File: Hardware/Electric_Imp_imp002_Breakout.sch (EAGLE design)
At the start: 42 parts, among them Q1 DMG2307L-7, Q2 PHOTOTRANSISTORPT17-21C-L41-T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, U1 imp002, U2 TPS62172, X1 USBSMD

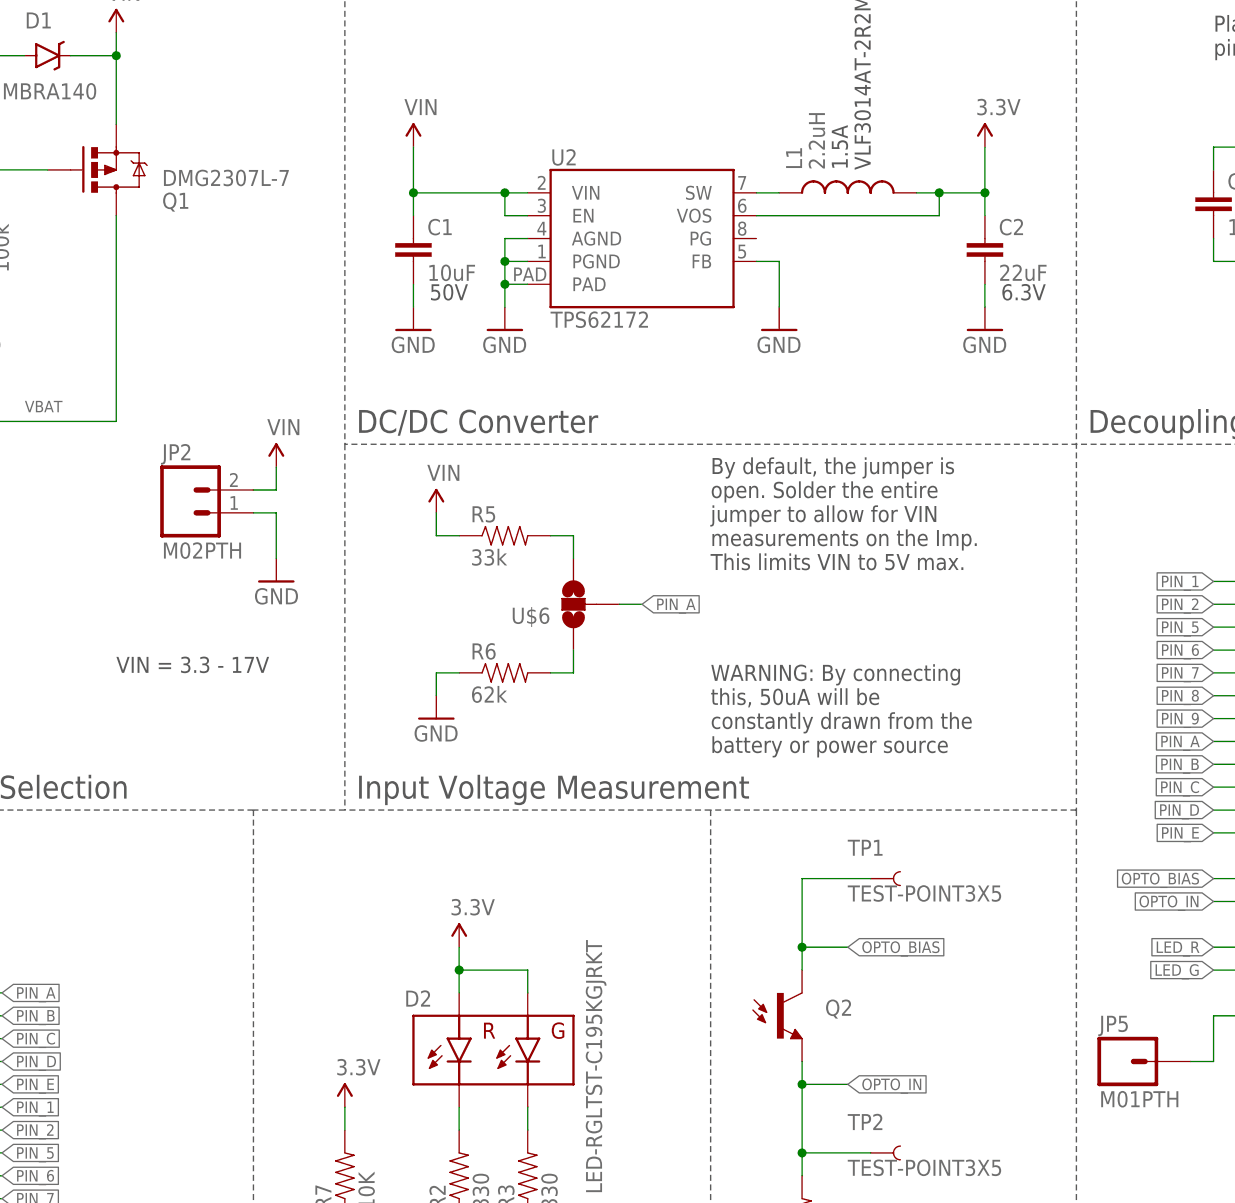
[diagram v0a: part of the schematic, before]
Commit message: Fixed 3-way jumper name. Added PROD_ID to components lacking it. Added device name to phototransistor in schematic.
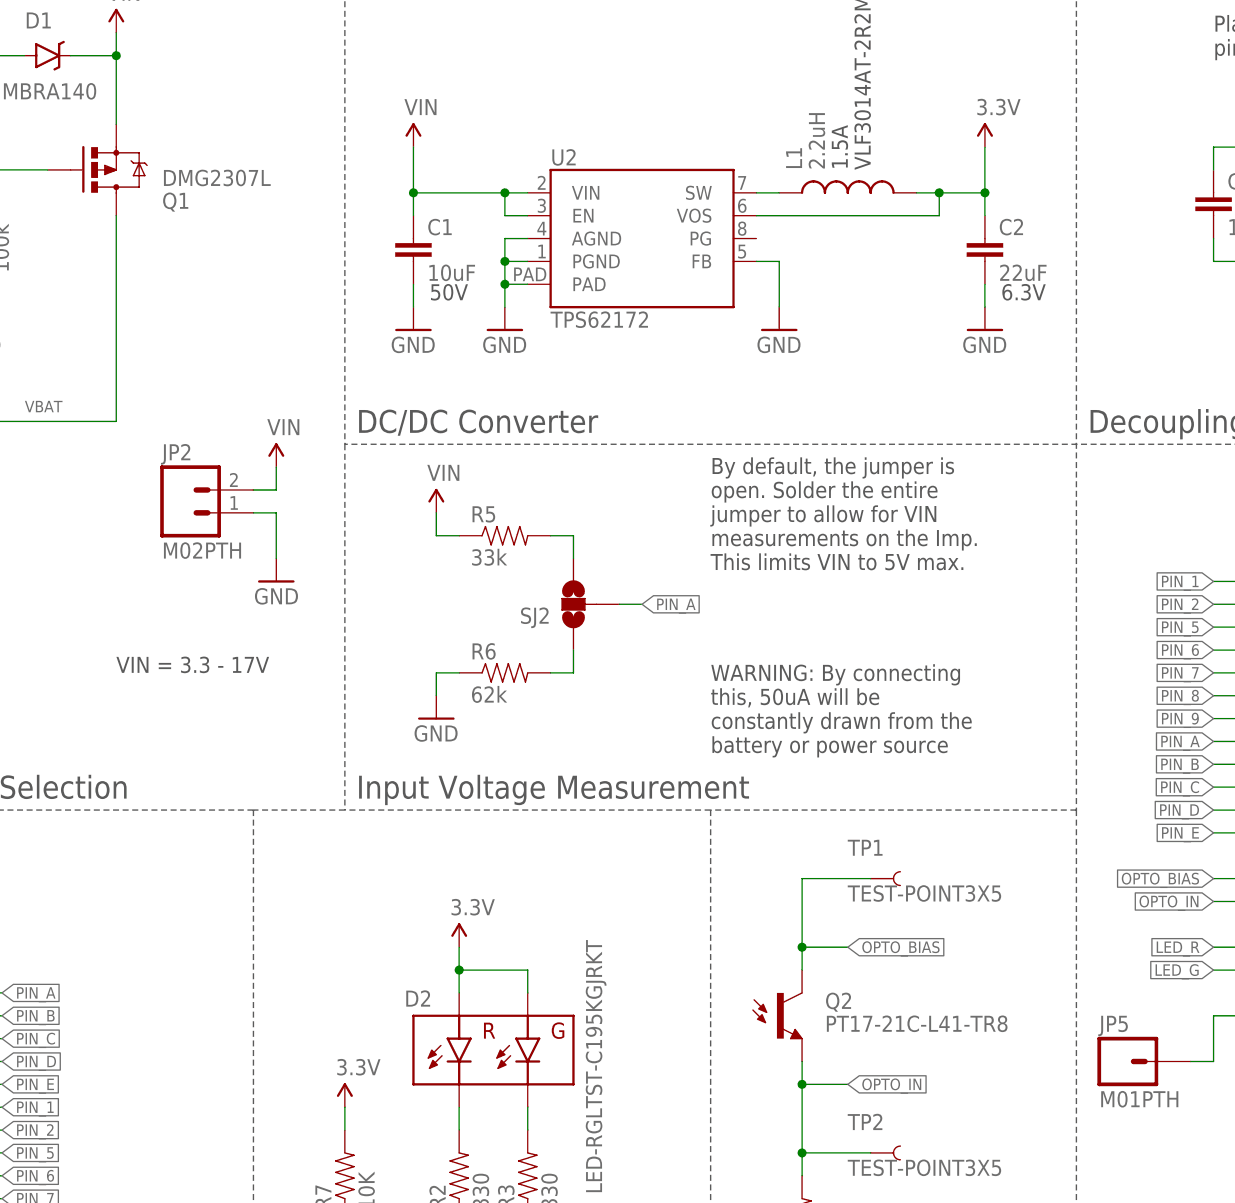
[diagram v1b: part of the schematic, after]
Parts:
- C2: PROD_ID (none) -> CAP-08402
- C3, C5, C7: PROD_ID (none) -> CAP-07883
- Q1: value DMG2307L-7 -> DMG2307L; device SparkFun-DiscreteSemi:MOSFET-PCHANNELSMD -> SparkFun-DiscreteSemi:MOSFET-PCHANNELDMG2307L
- Q2: DEVICE (none) -> PT17-21C-L41-TR8
- R6: PROD_ID (none) -> RES-09993
- renumbered U$6 to SJ2
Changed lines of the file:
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@@
 <part name="FRAME1" library="SparkFun-Aesthetics" deviceset="FRAME-LETTER" device=""/>
 <part name="U1" library="SparkFun-DigitalIC" deviceset="ELECTRIC_IMP_IMP002" device="" value="imp002"/>
-<part name="C2" library="SparkFun-Passives" deviceset="CAP" device="0805" value="22uF"/>
+<part name="C2" library="SparkFun-Passives" deviceset="CAP" device="0805" value="22uF">
+<attribute name="PROD_ID" value="CAP-08402"/>
+</part>
 <part name="L1" library="SparkFun-Passives" deviceset="INDUCTOR" device="VLF4012A" value="2.2uH"/>
 <part name="GND1" library="SparkFun-Aesthetics" deviceset="GND" device=""/>
@@
 <part name="JP4" library="SparkFun-Connectors" deviceset="M02" device="PTH" value="M02PTH"/>
 <part name="GND11" library="SparkFun-Aesthetics" deviceset="GND" device=""/>
-<part name="Q1" library="SparkFun-DiscreteSemi" deviceset="MOSFET-PCHANNEL" device="SMD" value="DMG2307L-7"/>
+<part name="Q1" library="SparkFun-DiscreteSemi" deviceset="MOSFET-PCHANNEL" device="DMG2307L" value="DMG2307L"/>
 <part name="JP3" library="SparkFun-Connectors" deviceset="M02" device="-JST-2MM-SMT" value="M02-JST-2MM-SMT"/>
 <part name="GND5" library="SparkFun-Aesthetics" deviceset="GND" device=""/>
 <part name="U$3" library="SparkFun-Aesthetics" deviceset="VIN" device=""/>
 <part name="GND6" library="SparkFun-Aesthetics" deviceset="GND" device=""/>
-<part name="C3" library="SparkFun-Capacitors" deviceset="CAP" device="0603-CAP" value="100pF"/>
+<part name="C3" library="SparkFun-Capacitors" deviceset="CAP" device="0603-CAP" value="100pF">
+<attribute name="PROD_ID" value="CAP-07883"/>
+</part>
 <part name="C4" library="SparkFun-Capacitors" deviceset="1.0UF-16V-10%(0603)" device="" value="1.0uF"/>
-<part name="C5" library="SparkFun-Capacitors" deviceset="CAP" device="0603-CAP" value="100pF"/>
+<part name="C5" library="SparkFun-Capacitors" deviceset="CAP" device="0603-CAP" value="100pF">
+<attribute name="PROD_ID" value="CAP-07883"/>
+</part>
 <part name="C6" library="SparkFun-Capacitors" deviceset="1.0UF-16V-10%(0603)" device="" value="1.0uF"/>
 <part name="GND7" library="SparkFun-Aesthetics" deviceset="GND" device=""/>
@@
 <part name="SJ1" library="SparkFun-Passives" deviceset="JUMPER-PAD-2-NC_BY_PASTE" device=""/>
 <part name="P+5" library="SparkFun-Aesthetics" deviceset="3.3V" device=""/>
-<part name="Q2" library="SparkFun-DiscreteSemi" deviceset="PHOTOTRANSISTOR" device="PT17-21C-L41-TR8"/>
+<part name="Q2" library="SparkFun-DiscreteSemi" deviceset="PHOTOTRANSISTOR" device="PT17-21C-L41-TR8">
+<attribute name="DEVICE" value="PT17-21C-L41-TR8"/>
+</part>
 <part name="D2" library="SparkFun-LED" deviceset="LED-RG" device="LTST-C195KGJRKT"/>
 <part name="R2" library="SparkFun-Resistors" deviceset="330OHM1/10W1%(0603)" device="" value="330"/>
@@
 <part name="U$7" library="SparkFun-Aesthetics" deviceset="VIN" device=""/>
 <part name="GND15" library="SparkFun-Aesthetics" deviceset="GND" device=""/>
-<part name="U$6" library="SparkFun-Passives" deviceset="JUMPER-PAD-3-NO" device="FULL_BOX_SILK"/>
+<part name="SJ2" library="SparkFun-Passives" deviceset="JUMPER-PAD-3-NO" device="FULL_BOX_SILK"/>
 <part name="R5" library="SparkFun-Resistors" deviceset="33KOHM1/10W1%(0603)" device="" value="33k"/>
-<part name="R6" library="SparkFun-Resistors" deviceset="RESISTOR" device="0603" value="62k"/>
+<part name="R6" library="SparkFun-Resistors" deviceset="RESISTOR" device="0603" value="62k">
+<attribute name="PROD_ID" value="RES-09993"/>
+</part>
 <part name="U$8" library="SparkFun-Aesthetics" deviceset="VIN" device=""/>
 <part name="GND10" library="SparkFun-Aesthetics" deviceset="GND" device=""/>
-<part name="C7" library="SparkFun-Capacitors" deviceset="CAP" device="0603-CAP" value="100pF"/>
+<part name="C7" library="SparkFun-Capacitors" deviceset="CAP" device="0603-CAP" value="100pF">
+<attribute name="PROD_ID" value="CAP-07883"/>
+</part>
 <part name="TP1" library="SparkFun-Passives" deviceset="TEST-POINT" device="3X5"/>
 <part name="TP2" library="SparkFun-Passives" deviceset="TEST-POINT" device="3X5"/>
@@
 <instance part="FRAME1" gate="G$2" x="147.32" y="0"/>
 <instance part="U1" gate="G$1" x="195.58" y="86.36"/>
-<instance part="C2" gate="G$1" x="144.78" y="144.78"/>
+<instance part="C2" gate="G$1" x="144.78" y="144.78">
+<attribute name="PROD_ID" x="144.78" y="144.78" size="1.778" layer="96" display="off"/>
+</instance>
 <instance part="L1" gate="G$1" x="129.54" y="152.4" smashed="yes" rot="R90">
 <attribute name="NAME" x="124.46" y="154.94" size="1.778" layer="95" rot="R90"/>
@@
 <instance part="U$3" gate="G$1" x="66.04" y="121.92"/>
 <instance part="GND6" gate="1" x="220.98" y="55.88" rot="MR0"/>
-<instance part="C3" gate="G$1" x="170.18" y="149.86"/>
+<instance part="C3" gate="G$1" x="170.18" y="149.86">
+<attribute name="PROD_ID" x="170.18" y="149.86" size="1.778" layer="96" display="off"/>
+</instance>
 <instance part="C4" gate="G$1" x="180.34" y="149.86"/>
-<instance part="C5" gate="G$1" x="193.04" y="149.86"/>
+<instance part="C5" gate="G$1" x="193.04" y="149.86">
+<attribute name="PROD_ID" x="193.04" y="149.86" size="1.778" layer="96" display="off"/>
+</instance>
 <instance part="C6" gate="G$1" x="203.2" y="149.86"/>
 <instance part="GND7" gate="1" x="180.34" y="139.7" rot="MR0"/>
@@
 <instance part="P+5" gate="G$1" x="220.98" y="116.84"/>
 <instance part="Q2" gate="G$1" x="121.92" y="60.96" smashed="yes">
-<attribute name="NAME" x="127" y="60.96" size="1.778" layer="95"/>
+<attribute name="NAME" x="127" y="61.722" size="1.778" layer="95"/>
+<attribute name="DEVICE" x="127" y="59.182" size="1.778" layer="96"/>
 </instance>
 <instance part="D2" gate="G$1" x="88.9" y="58.42" smashed="yes">
@@
 <instance part="U$7" gate="G$1" x="48.26" y="170.18"/>
 <instance part="GND15" gate="1" x="33.02" y="137.16"/>
-<instance part="U$6" gate="G$1" x="99.06" y="106.68" smashed="yes" rot="R180">
+<instance part="SJ2" gate="G$1" x="99.06" y="106.68" smashed="yes" rot="R180">
 <attribute name="NAME" x="96.52" y="106.299" size="1.778" layer="95" rot="R180"/>
 </instance>
 <instance part="R5" gate="G$1" x="91.44" y="114.3"/>
-<instance part="R6" gate="G$1" x="91.44" y="99.06"/>
+<instance part="R6" gate="G$1" x="91.44" y="99.06">
+<attribute name="PROD_ID" x="91.44" y="99.06" size="1.778" layer="96" display="off"/>
+</instance>
 <instance part="U$8" gate="G$1" x="83.82" y="116.84"/>
 <instance part="GND10" gate="1" x="83.82" y="93.98"/>
-<instance part="C7" gate="G$1" x="215.9" y="149.86"/>
+<instance part="C7" gate="G$1" x="215.9" y="149.86">
+<attribute name="PROD_ID" x="215.9" y="149.86" size="1.778" layer="96" display="off"/>
+</instance>
 <instance part="TP1" gate="G$1" x="132.08" y="76.2"/>
 <instance part="TP2" gate="G$1" x="132.08" y="45.72"/>
@@
 </segment>
 <segment>
-<pinref part="U$6" gate="G$1" pin="2"/>
+<pinref part="SJ2" gate="G$1" pin="2"/>
 <wire x1="104.14" y1="106.68" x2="106.68" y2="106.68" width="0.1524" layer="91"/>
 <label x="106.68" y="106.68" size="1.27" layer="95" xref="yes"/>
@@
 <segment>
 <pinref part="R5" gate="G$1" pin="2"/>
-<pinref part="U$6" gate="G$1" pin="3"/>
+<pinref part="SJ2" gate="G$1" pin="3"/>
 <wire x1="96.52" y1="114.3" x2="99.06" y2="114.3" width="0.1524" layer="91"/>
 <wire x1="99.06" y1="114.3" x2="99.06" y2="111.76" width="0.1524" layer="91"/>
@@
 <net name="N$7" class="0">
 <segment>
-<pinref part="U$6" gate="G$1" pin="1"/>
+<pinref part="SJ2" gate="G$1" pin="1"/>
 <wire x1="99.06" y1="101.6" x2="99.06" y2="99.06" width="0.1524" layer="91"/>
 <pinref part="R6" gate="G$1" pin="2"/>

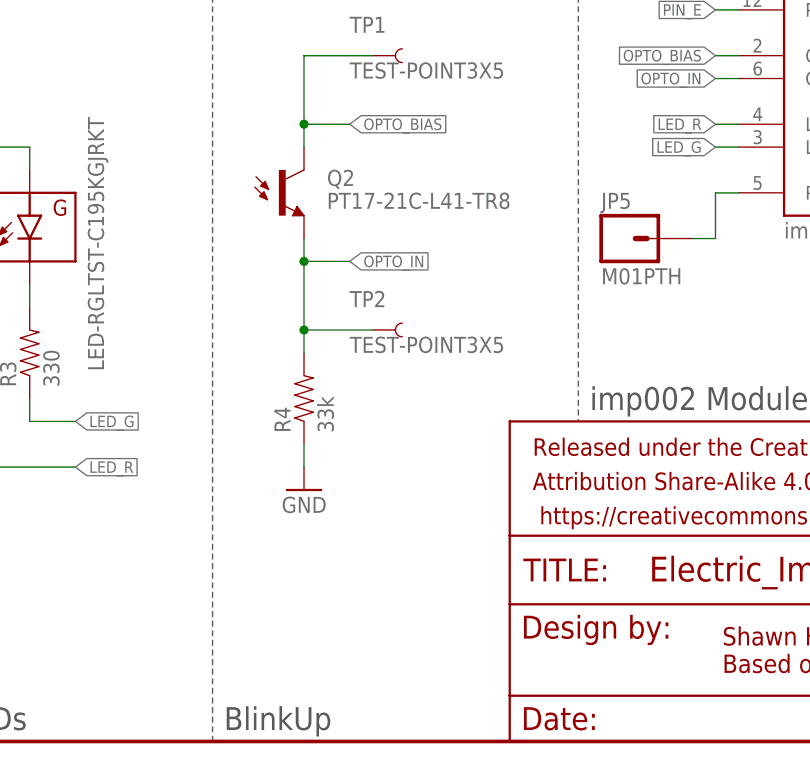
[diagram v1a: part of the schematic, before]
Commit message: Fixed issues from GitHub for reds.
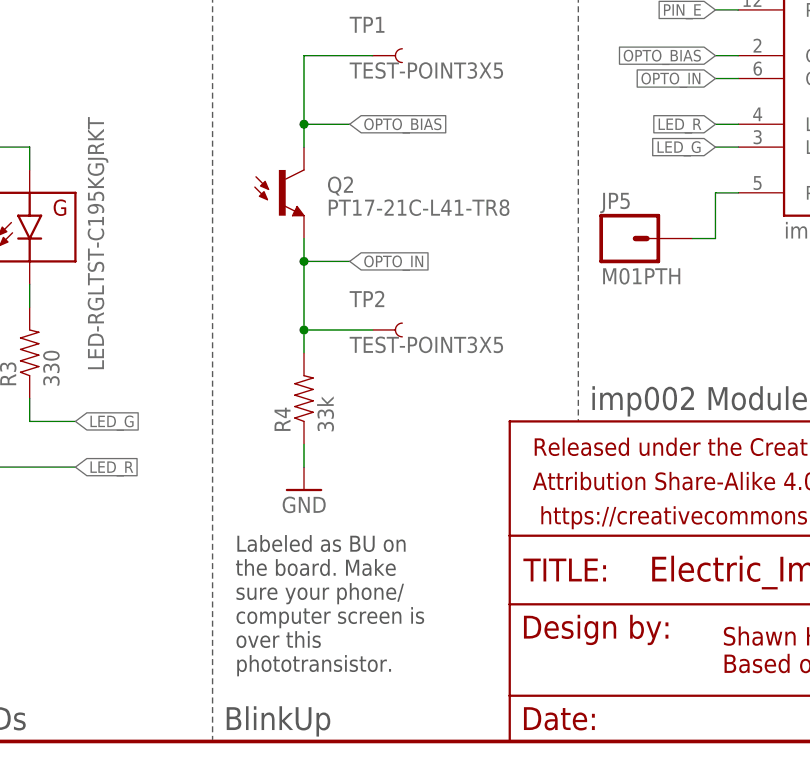
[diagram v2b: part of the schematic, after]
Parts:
- Q2: value PHOTOTRANSISTORPT17-21C-L41-TR8 -> PT17-21C-L41-TR8; DEVICE PT17-21C-L41-TR8 -> (none)
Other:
- note added: "Labeled as BU on the board. Make sure your phone/ computer screen is over this phototransistor."
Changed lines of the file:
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@@
 <part name="SJ1" library="SparkFun-Passives" deviceset="JUMPER-PAD-2-NC_BY_PASTE" device=""/>
 <part name="P+5" library="SparkFun-Aesthetics" deviceset="3.3V" device=""/>
-<part name="Q2" library="SparkFun-DiscreteSemi" deviceset="PHOTOTRANSISTOR" device="PT17-21C-L41-TR8">
-<attribute name="DEVICE" value="PT17-21C-L41-TR8"/>
-</part>
+<part name="Q2" library="SparkFun-DiscreteSemi" deviceset="PHOTOTRANSISTOR" device="PT17-21C-L41-TR8" value="PT17-21C-L41-TR8"/>
 <part name="D2" library="SparkFun-LED" deviceset="LED-RG" device="LTST-C195KGJRKT"/>
 <part name="R2" library="SparkFun-Resistors" deviceset="330OHM1/10W1%(0603)" device="" value="330"/>
@@
 it could damage
 the Imp</text>
+<text x="116.84" y="22.86" size="1.778" layer="97" align="top-left">Labeled as BU on
+the board. Make
+sure your phone/
+computer screen is
+over this
+phototransistor.</text>
 </plain>
 <instances>
@@
 </instance>
 <instance part="P+5" gate="G$1" x="220.98" y="116.84"/>
-<instance part="Q2" gate="G$1" x="121.92" y="60.96" smashed="yes">
-<attribute name="NAME" x="127" y="61.722" size="1.778" layer="95"/>
-<attribute name="DEVICE" x="127" y="59.182" size="1.778" layer="96"/>
-</instance>
+<instance part="Q2" gate="G$1" x="121.92" y="60.96"/>
 <instance part="D2" gate="G$1" x="88.9" y="58.42" smashed="yes">
 <attribute name="NAME" x="80.264" y="61.976" size="1.778" layer="95"/>

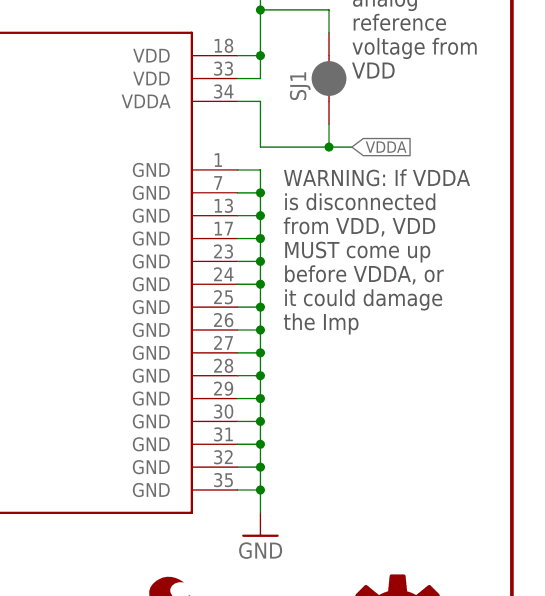
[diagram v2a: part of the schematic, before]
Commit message: Fixed note about VDD/VDDA jumper in schematic.
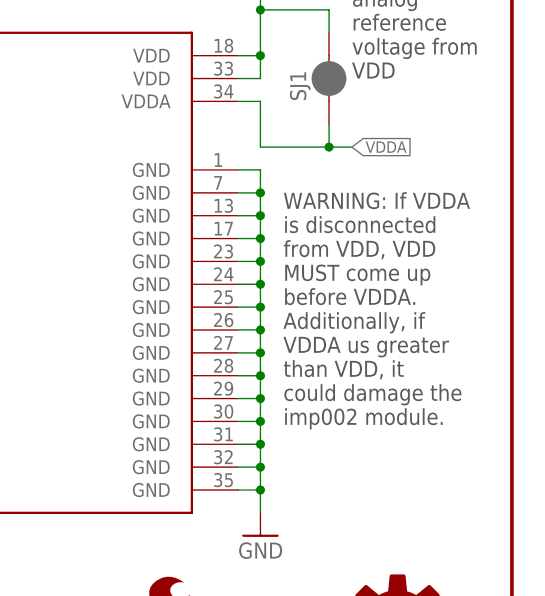
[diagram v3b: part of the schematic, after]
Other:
- note added: "WARNING: If VDDA is disconnected from VDD, VDD MUST come up before VDDA. Additionally, if VDDA us greater than VDD, it could damage the imp002 module."
- note removed: "WARNING: If VDDA is disconnected from VDD, VDD MUST come up before VDDA, or it could damage the Imp"
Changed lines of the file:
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@@
 <?xml version="1.0" encoding="utf-8"?>
 <!DOCTYPE eagle SYSTEM "eagle.dtd">
-<eagle version="6.5.0">
+<eagle version="7.2.0">
 <drawing>
 <settings>
@@
 <setting verticaltext="up"/>
 </settings>
-<grid distance="0.1" unitdist="inch" unit="inch" style="lines" multiple="1" display="yes" altdistance="0.01" altunitdist="inch" altunit="inch"/>
+<grid distance="0.1" unitdist="inch" unit="inch" style="lines" multiple="1" display="no" altdistance="0.01" altunitdist="inch" altunit="inch"/>
 <layers>
 <layer number="1" name="Top" color="4" fill="1" visible="no" active="no"/>
@@
 constantly drawn from the
 battery or power source</text>
-<text x="223.52" y="78.74" size="1.778" layer="97">WARNING: If VDDA
+<text x="223.52" y="93.98" size="1.778" layer="97" align="top-left">WARNING: If VDDA
 is disconnected
 from VDD, VDD
 MUST come up
-before VDDA, or
-it could damage
-the Imp</text>
+before VDDA.
+Additionally, if
+VDDA us greater
+than VDD, it
+could damage the
+imp002 module.</text>
 <text x="116.84" y="22.86" size="1.778" layer="97" align="top-left">Labeled as BU on
 the board. Make
